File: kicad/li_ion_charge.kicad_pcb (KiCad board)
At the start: 2 copper layers, 18 parts, among them P101 USB_B, P102 CONN_01X02, P103 CONN_01X02, U101 MCP73834-FCI/UN

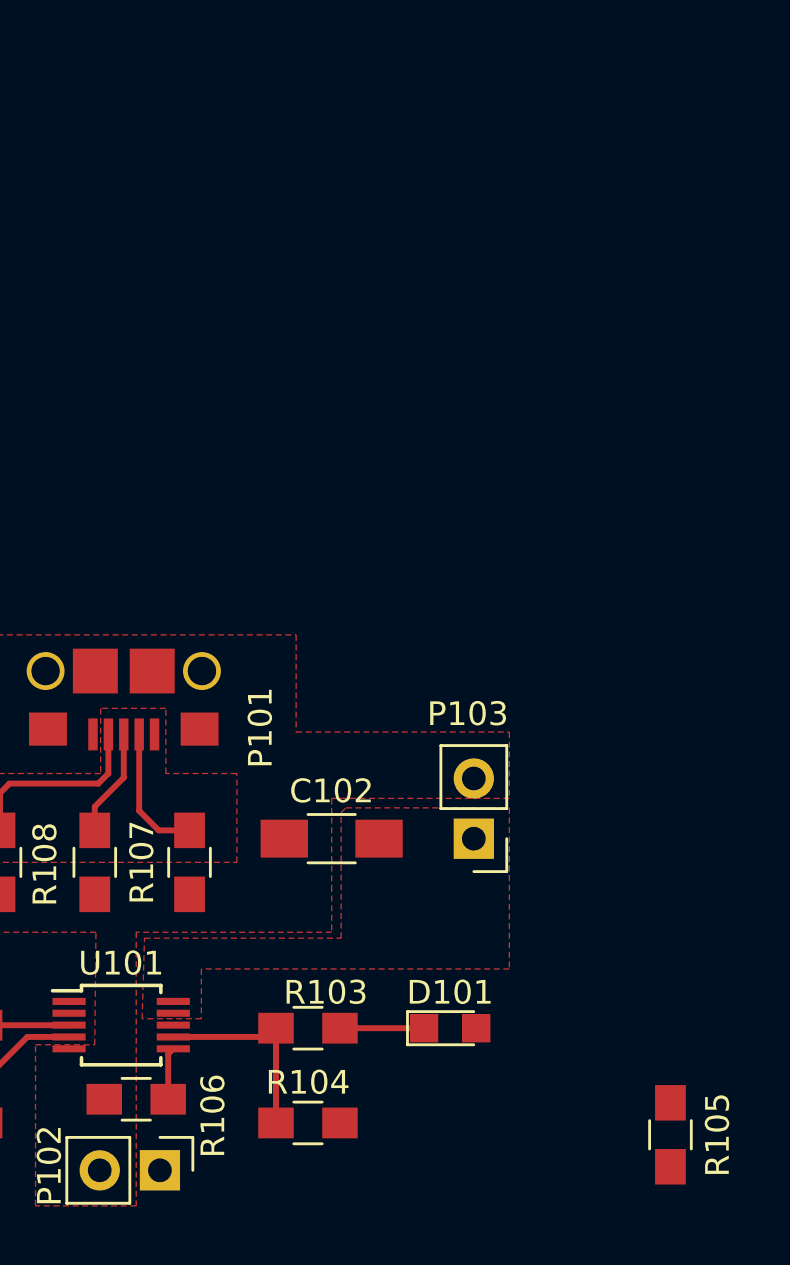
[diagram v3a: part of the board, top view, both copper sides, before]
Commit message: Add data sheet for MCP738334
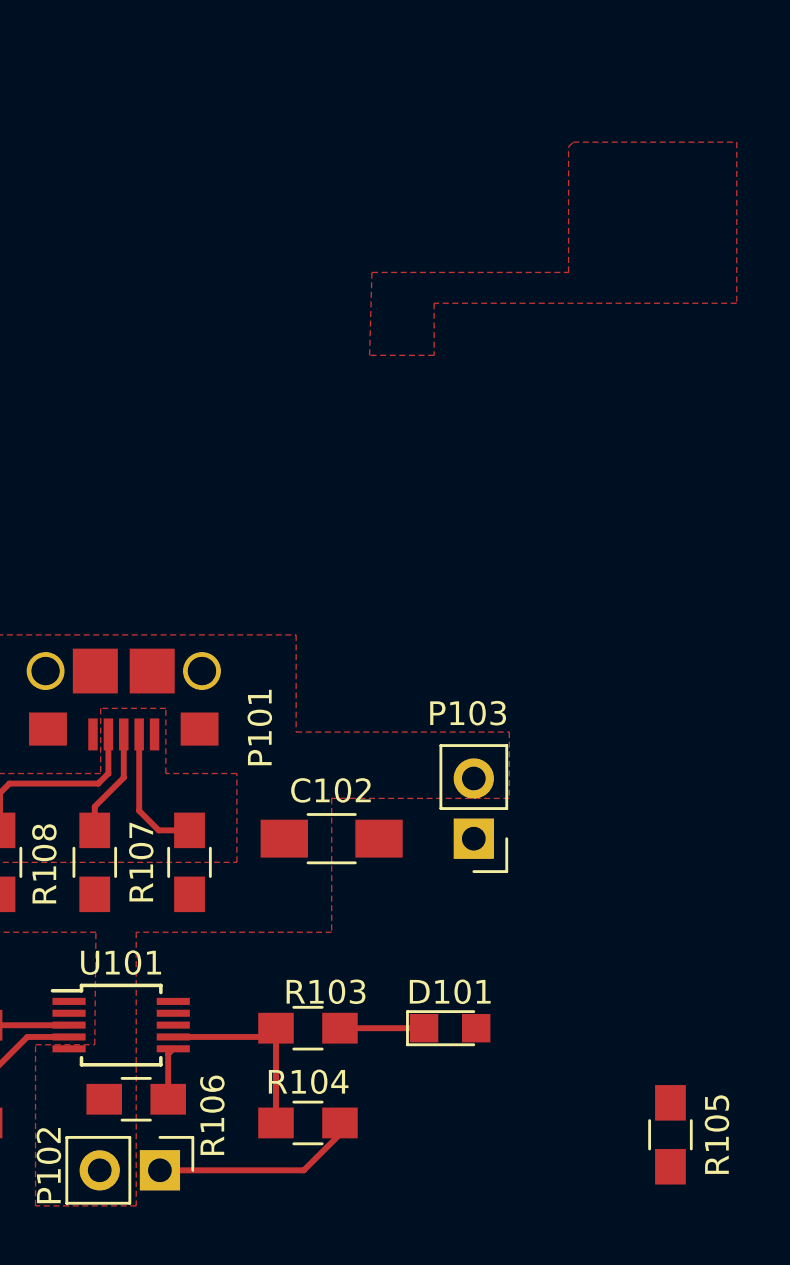
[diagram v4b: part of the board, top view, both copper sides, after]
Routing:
- net /RESET: track 0.00 -> 8.71 mm
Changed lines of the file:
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@@
   (general
     (links 38)
-    (no_connects 10)
+    (no_connects 11)
     (area 0 0 0 0)
     (thickness 1.6)
     (drawings 0)
-    (tracks 26)
+    (tracks 29)
     (zones 0)
     (modules 18)
@@
   (segment (start 86.3396 44.0503) (end 86.3396 44.7396) (width 0.25) (layer F.Cu) (net 0))
   (segment (start 96.6 58.05) (end 96.4 58.25) (width 0.25) (layer F.Cu) (net 0))
-  (segment (start 167.35 103) (end 170.9 103) (width 0.25) (layer F.Cu) (net 2) (status C00000))
-  (segment (start 146.1 107) (end 149.65 107) (width 0.25) (layer F.Cu) (net 3) (status C00000))
-  (segment (start 146.1 102.875) (end 149.65 102.875) (width 0.25) (layer F.Cu) (net 4) (status C00000))
-  (segment (start 158.225 90.6) (end 158.225 92.425) (width 0.25) (layer F.Cu) (net 5) (status 400000))
-  (segment (start 157 93.65) (end 157 94.65) (width 0.25) (layer F.Cu) (net 5) (status 800000))
+  (segment (start 167.35 103) (end 170.9 103) (width 0.25) (layer F.Cu) (net 2))
+  (segment (start 146.1 107) (end 149.65 107) (width 0.25) (layer F.Cu) (net 3))
+  (segment (start 146.1 102.875) (end 149.65 102.875) (width 0.25) (layer F.Cu) (net 4))
+  (segment (start 158.225 90.6) (end 158.225 92.425) (width 0.25) (layer F.Cu) (net 5))
+  (segment (start 157 93.65) (end 157 94.65) (width 0.25) (layer F.Cu) (net 5))
   (segment (start 158.225 92.425) (end 157 93.65) (width 0.25) (layer F.Cu) (net 5))
-  (segment (start 158.875 90.6) (end 158.875 93.825) (width 0.25) (layer F.Cu) (net 6) (status 400000))
-  (segment (start 159.7 94.65) (end 161 94.65) (width 0.25) (layer F.Cu) (net 6) (status 800000))
+  (segment (start 158.875 90.6) (end 158.875 93.825) (width 0.25) (layer F.Cu) (net 6))
+  (segment (start 159.7 94.65) (end 161 94.65) (width 0.25) (layer F.Cu) (net 6))
   (segment (start 158.875 93.825) (end 159.7 94.65) (width 0.25) (layer F.Cu) (net 6))
-  (segment (start 164.65 107) (end 164.65 103) (width 0.25) (layer F.Cu) (net 10) (status C00000))
-  (segment (start 164.65 103) (end 164.28 103.37) (width 0.25) (layer F.Cu) (net 10) (status C00000))
-  (segment (start 164.28 103.37) (end 160.315 103.37) (width 0.25) (layer F.Cu) (net 10) (status C00000))
-  (segment (start 160.1 106) (end 160.1 104.085) (width 0.25) (layer F.Cu) (net 12) (status 400000))
-  (segment (start 160.1 104.085) (end 160.315 103.87) (width 0.25) (layer F.Cu) (net 12) (status 800000))
+  (segment (start 167.35 107) (end 167.35 107.475) (width 0.25) (layer F.Cu) (net 9))
+  (segment (start 167.35 107.475) (end 165.825 109) (width 0.25) (layer F.Cu) (net 9))
+  (segment (start 165.825 109) (end 159.75 109) (width 0.25) (layer F.Cu) (net 9))
+  (segment (start 164.65 107) (end 164.65 103) (width 0.25) (layer F.Cu) (net 10))
+  (segment (start 164.65 103) (end 164.28 103.37) (width 0.25) (layer F.Cu) (net 10))
+  (segment (start 164.28 103.37) (end 160.315 103.37) (width 0.25) (layer F.Cu) (net 10))
+  (segment (start 160.1 106) (end 160.1 104.085) (width 0.25) (layer F.Cu) (net 12))
+  (segment (start 160.1 104.085) (end 160.315 103.87) (width 0.25) (layer F.Cu) (net 12))
   (segment (start 152.35 102.875) (end 155.91 102.875) (width 0.25) (layer F.Cu) (net 13))
   (segment (start 155.91 102.875) (end 155.915 102.87) (width 0.25) (layer F.Cu) (net 13))
-  (segment (start 155.915 103.37) (end 154.155 103.37) (width 0.25) (layer F.Cu) (net 14) (status 400000))
-  (segment (start 152.35 105.175) (end 152.35 107) (width 0.25) (layer F.Cu) (net 14) (status 800000))
+  (segment (start 155.915 103.37) (end 154.155 103.37) (width 0.25) (layer F.Cu) (net 14))
+  (segment (start 152.35 105.175) (end 152.35 107) (width 0.25) (layer F.Cu) (net 14))
   (segment (start 154.155 103.37) (end 152.35 105.175) (width 0.25) (layer F.Cu) (net 14))
-  (segment (start 157.575 90.6) (end 157.575 92.25) (width 0.25) (layer F.Cu) (net 15) (status 400000))
-  (segment (start 153 93.075) (end 153 94.65) (width 0.25) (layer F.Cu) (net 15) (status 800000))
+  (segment (start 157.575 90.6) (end 157.575 92.25) (width 0.25) (layer F.Cu) (net 15))
+  (segment (start 153 93.075) (end 153 94.65) (width 0.25) (layer F.Cu) (net 15))
   (segment (start 153.4 92.675) (end 153 93.075) (width 0.25) (layer F.Cu) (net 15))
   (segment (start 157.15 92.675) (end 153.4 92.675) (width 0.25) (layer F.Cu) (net 15))
@@
     (polygon
       (pts
-        (xy 167.6 93.7) (xy 174.5 93.7) (xy 174.5 100.5) (xy 161.5 100.5) (xy 161.5 102.6)
-        (xy 159 102.6) (xy 159.1 99.2) (xy 167.4 99.2) (xy 167.4 93.9)
+        (xy 177.2 65.6) (xy 184.1 65.6) (xy 184.1 72.4) (xy 171.325 72.4) (xy 171.325 74.6)
+        (xy 168.6 74.6) (xy 168.7 71.1) (xy 177 71.1) (xy 177 65.8)
       )
     )

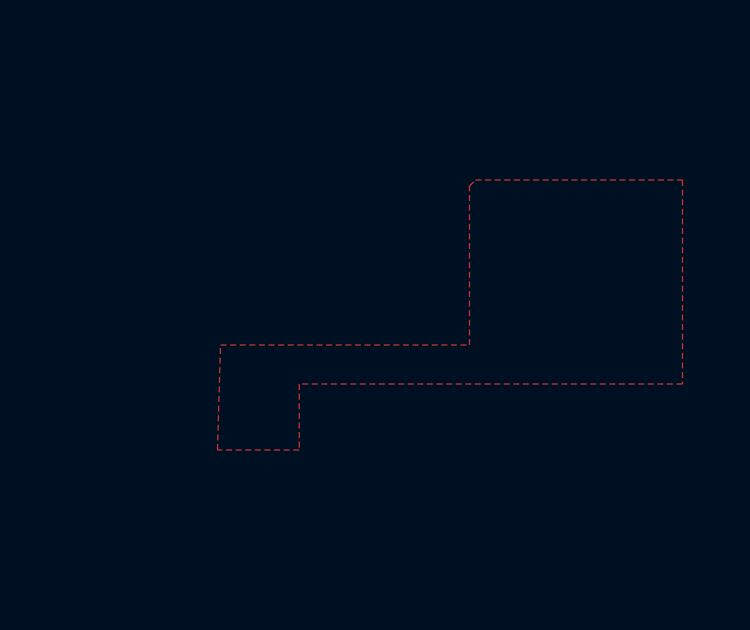
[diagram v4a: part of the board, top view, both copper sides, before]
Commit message: Add initial osh part design rule defaults
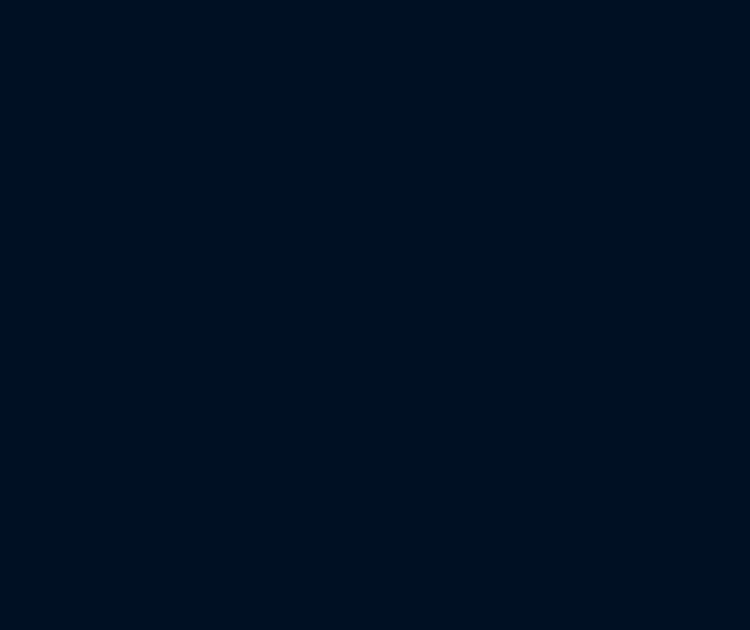
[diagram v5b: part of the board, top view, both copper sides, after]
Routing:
- removed copper zone on F.Cu, net /VBAT
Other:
- net class Default: clearance 0.2 -> 0.254; trace_width 0.25 -> 0.254; via_dia 0.6 -> 0.889; via_drill 0.4 -> 0.635
- rule trace_clearance: 0.2 -> 0.254
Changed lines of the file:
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@@
   (general
     (links 38)
-    (no_connects 11)
-    (area 0 0 0 0)
+    (no_connects 12)
+    (area 86.014599 43.725299 184.375 114.033333)
     (thickness 1.6)
     (drawings 0)
@@
   )
   (setup
-    (last_trace_width 0.25)
-    (trace_clearance 0.2)
+    (last_trace_width 0.254)
+    (trace_clearance 0.254)
     (zone_clearance 0.2032)
     (zone_45_only no)
@@
     (segment_width 0.2)
     (edge_width 0.15)
-    (via_size 0.6)
-    (via_drill 0.4)
+    (via_size 0.889)
+    (via_drill 0.635)
     (via_min_size 0.4)
     (via_min_drill 0.3)
@@
     (uvia_drill 0.1)
     (uvias_allowed no)
-    (uvia_min_size 0.2)
-    (uvia_min_drill 0.1)
+    (uvia_min_size 0)
+    (uvia_min_drill 0)
     (pcb_text_width 0.3)
     (pcb_text_size 1.5 1.5)
@@
   (net 15 "Net-(P101-Pad4)")
   (net_class Default "This is the default net class."
-    (clearance 0.2)
-    (trace_width 0.25)
-    (via_dia 0.6)
-    (via_drill 0.4)
+    (clearance 0.254)
+    (trace_width 0.254)
+    (via_dia 0.889)
+    (via_drill 0.635)
     (uvia_dia 0.3)
     (uvia_drill 0.1)
@@
       )
     )
-  )
-  (zone (net 7) (net_name /VBAT) (layer F.Cu) (hatch edge 0.508)
-    (connect_pads (clearance 0.2032))
-    (min_thickness 0.254)
-    (fill yes (arc_segments 16) (thermal_gap 0.254) (thermal_bridge_width 0.508))
-    (polygon
-      (pts
-        (xy 177.2 65.6) (xy 184.1 65.6) (xy 184.1 72.4) (xy 171.325 72.4) (xy 171.325 74.6)
-        (xy 168.6 74.6) (xy 168.7 71.1) (xy 177 71.1) (xy 177 65.8)
-      )
-    )

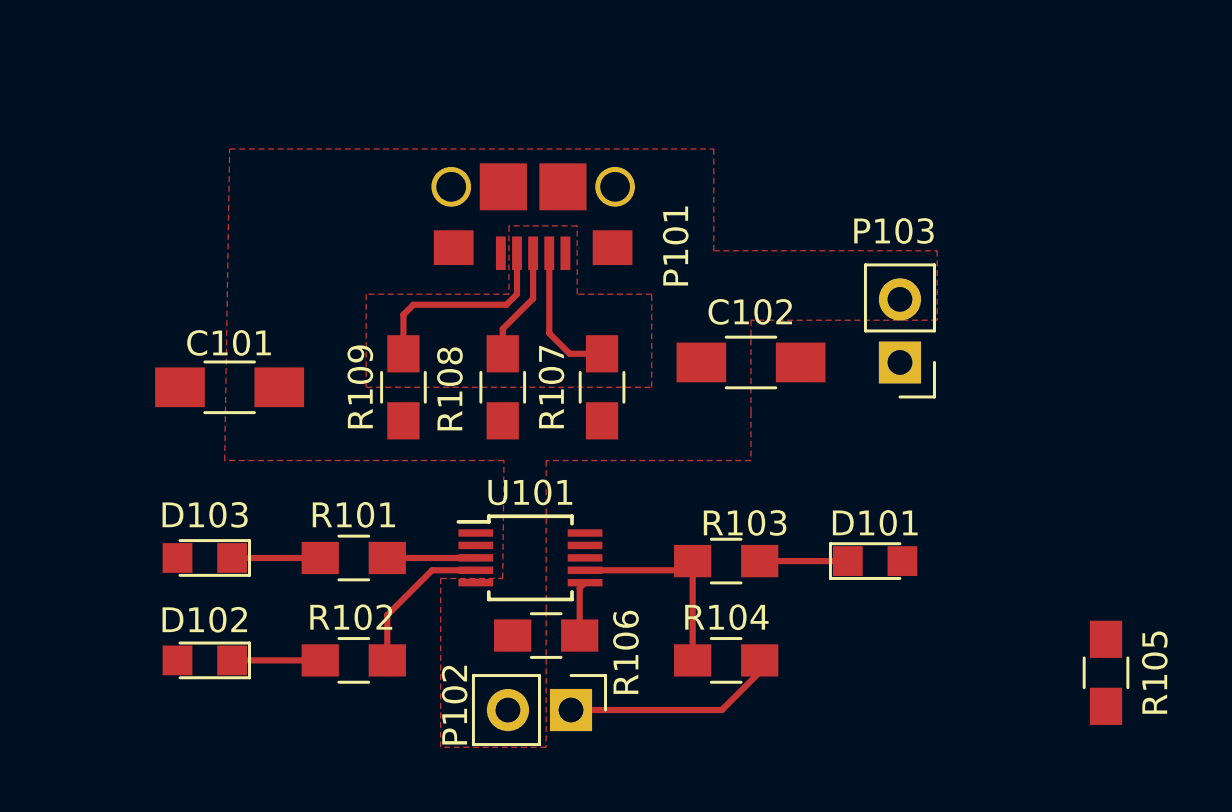
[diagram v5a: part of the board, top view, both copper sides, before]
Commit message: Front side planes and traces added
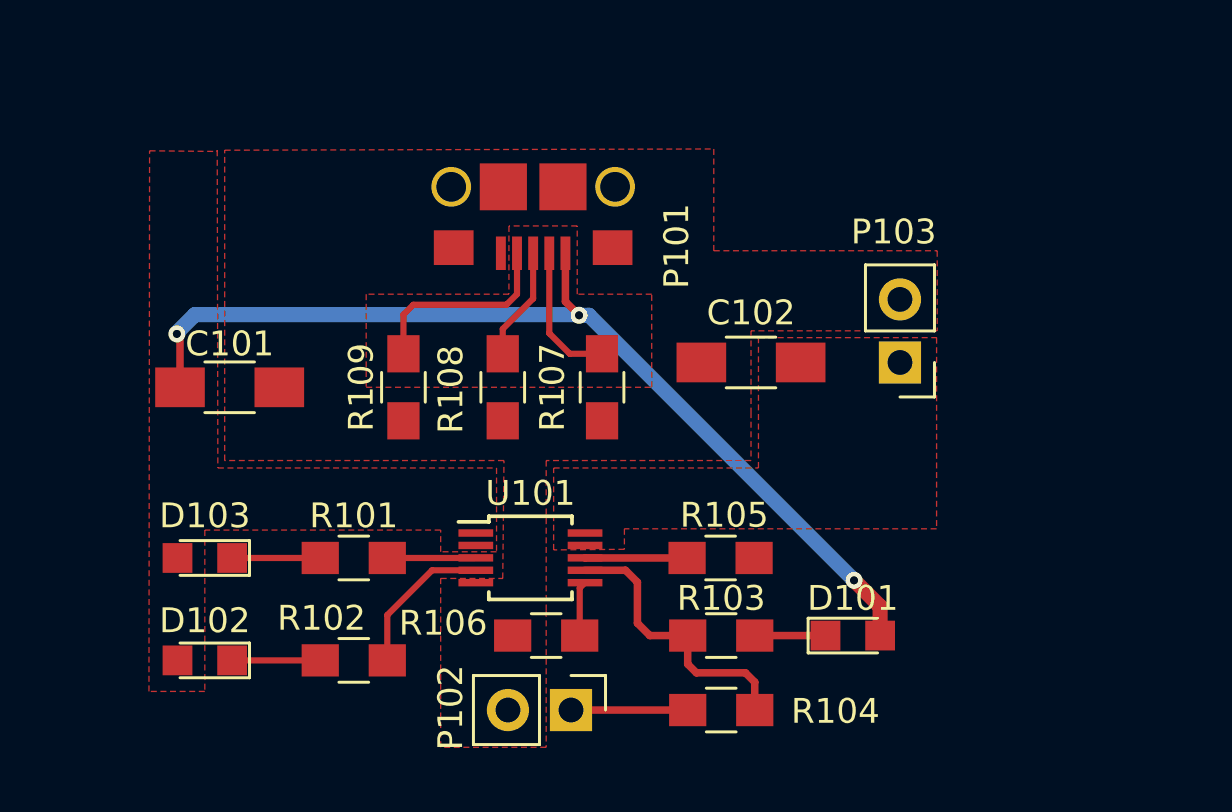
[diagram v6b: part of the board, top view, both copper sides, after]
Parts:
- moved R105 16.2 mm to (165.8, 102.9), turned to 180 degrees
- moved D101 3.13 mm to (171.1, 106.0)
- moved R103 3.01 mm to (165.8, 106.0)
- moved R104 2.01 mm to (165.8, 109.0), turned to 180 degrees
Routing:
- net /VIN: track 0.00 -> 39.6 mm, vias 0 -> 3
- net /Ther: track 0.00 -> 4.11 mm
- net /RESET: track 8.71 -> 4.70 mm
- net /~TE: track 8.49 -> 11.5 mm
- net Net-(D101-Pad1): track 3.55 -> 2.85 mm
- added copper zone on F.Cu, net /VBAT
- added copper zone on F.Cu, net /VIN
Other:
- net class Default: clearance 0.254 -> 0.1524; trace_width 0.254 -> 0.1524; via_dia 0.889 -> 0.6858; via_drill 0.635 -> 0.3302
- rule pad_to_mask_clearance: 0.2 -> 0
- rule trace_clearance: 0.254 -> 0.1524
- rule trace_min: 0.2 -> 0.1524
- rule via_min_drill: 0.3 -> 0.3302
- rule via_min_size: 0.4 -> 0.6858
